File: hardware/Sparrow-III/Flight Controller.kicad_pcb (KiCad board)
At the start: 4 copper layers, 40 x 40 mm, 89 parts

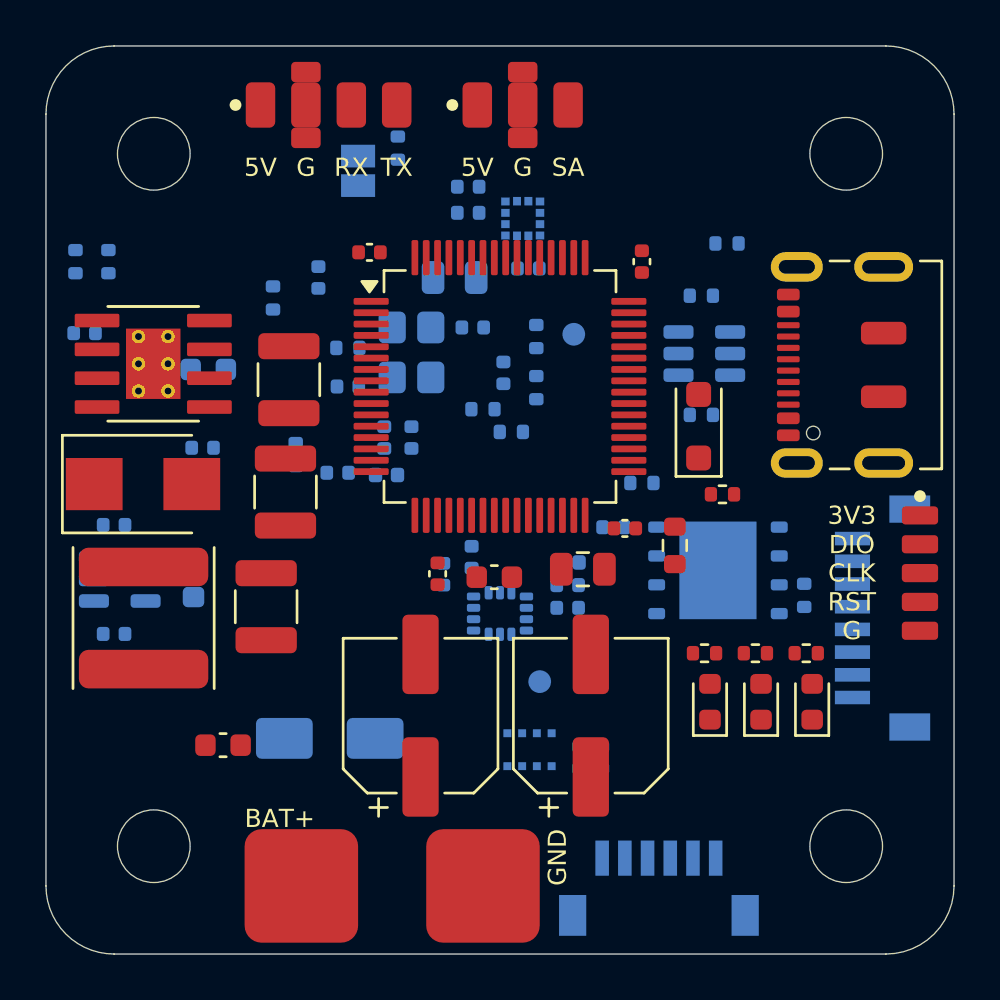
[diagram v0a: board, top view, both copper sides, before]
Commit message: WIP: uncommitted changes, moved to the cloud
Snapshot of the working tree the Claude desktop app took to continue
this session in the cloud. It was never committed on the desktop; fold
it into your next commit (git commit --amend) or unstage it
(git reset --mixed HEAD~1) before committing for real.
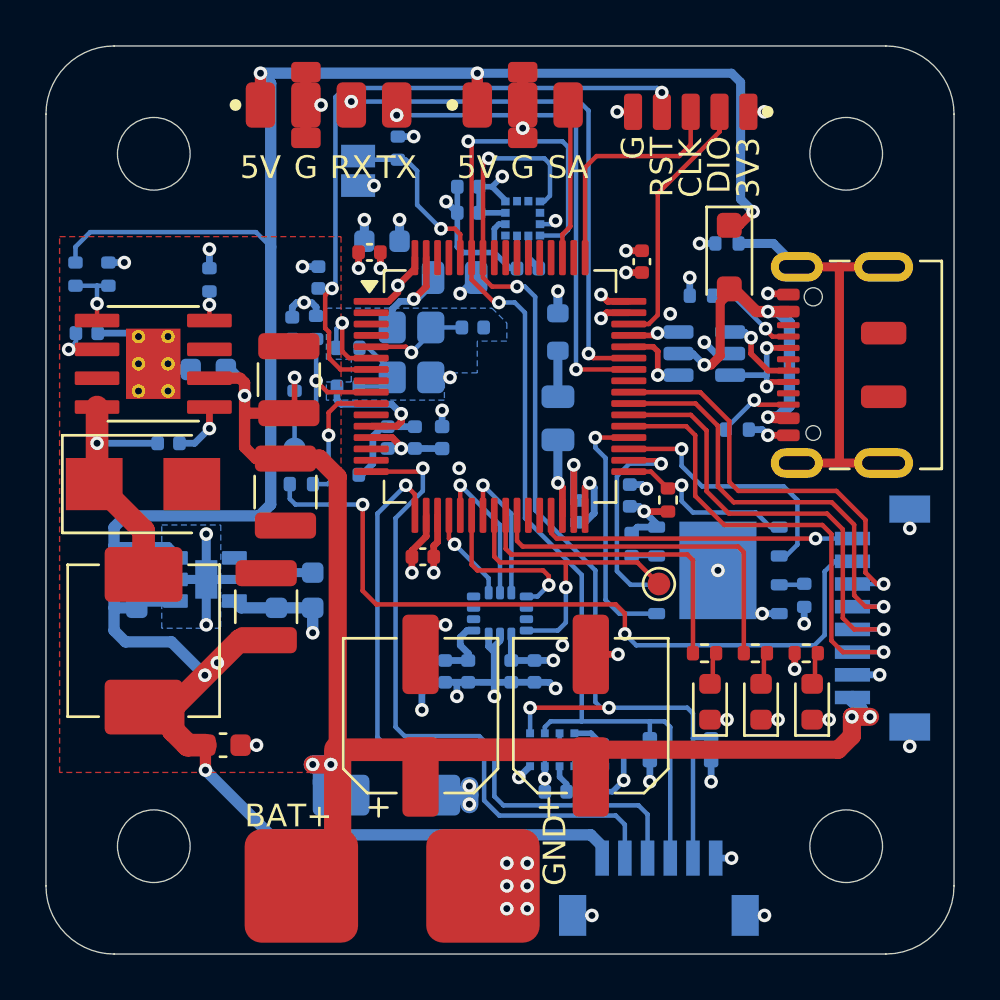
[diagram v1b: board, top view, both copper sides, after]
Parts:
- C_BUCK_OUT1: value 47uF -> 100uF
- C_LDO_IN1, C_LDO_OUT1: value 1uF -> 2.2uF; footprint Capacitor_SMD:C_0402_1005Metric -> Capacitor_SMD:C_0603_1608Metric
- C_MAG_BULK1: value 10uF -> 22uF
- C_VCAP1, C_VDD3, C_VDD_BULK1, R_VCAP_ESR1: moved to B.Cu
- D_TVS1: value SMAJ28A -> SMAJ26A
- L_BUCK1: footprint SparrowHawk:L_Sunlord_SWPA6028S -> SparrowHawk:L_Vishay_IHLP-2525CZ-01
- TP_IMU_INT_0: moved to F.Cu
- U_BARO1: value DPS310 -> DPS368
- U_LDO1: value AP2112K-3.3TRG1 -> TLV75533PDYDR; footprint Package_TO_SOT_SMD:SOT-23-5 -> SparrowHawk:SOT-23-5_ThermalPad_TI_DYD0005A
- Y_HSE1: value 8MHz CL=10pF ESR<150R -> 8MHz
- moved J_SWD1 22.7 mm to (158.4, 82.9), turned to 180 degrees
- moved R_I2C_SDA1 16.7 mm to (156.6, 111.0), turned to -90 degrees
- moved R_I2C_SCL1 16.5 mm to (159.3, 111.0), turned to 90 degrees
- moved C_VDD_BULK1 15.6 mm to (144.8, 88.6), turned to 180 degrees
- moved TP_VBAT_ADC_0 13.3 mm to (140.9, 97.8)
- moved R_VBAT_D1 11.0 mm to (140.9, 95.7)
- moved R_VCAP_ESR1 10.7 mm to (152.6, 92.6)
- moved R_VBAT_D2 10.1 mm to (141.9, 92.4)
- moved C_VBAT_ADC1 9.51 mm to (140.8, 92.4)
- moved FB_IMU1 8.03 mm to (146.6, 107.5), turned to -90 degrees
- moved D_USB_VBUS1 7.57 mm to (160.1, 89.3), turned to -90 degrees
- moved C_LDO_OUT1 7.40 mm to (140.2, 104.0), turned to 90 degrees
- moved TP_IMU_INT_0 6.79 mm to (157.0, 103.7)
- moved C_VCAP1 6.74 mm to (152.6, 96.4), turned to 90 degrees
- moved C_IMU_VDD1 6.08 mm to (147.6, 107.5), turned to -90 degrees
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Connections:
- U_LDO1 pad 4: GND -> unconnected-(U_LDO1-NC-Pad4)
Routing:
- net +5V: track 0.00 -> 113.4 mm, vias 0 -> 6
- net GND: track 0.00 -> 98.5 mm, vias 0 -> 57
- net VBAT: track 0.00 -> 59.5 mm, vias 0 -> 6
- net /MCU Core/I2C1_SDA: track 0.00 -> 50.2 mm, vias 0 -> 2
- net /MCU Core/I2C1_SCL: track 0.00 -> 48.0 mm, vias 0 -> 4
- net +3V3: track 0.00 -> 42.9 mm, vias 0 -> 22
- net /Interfaces&IO/ESC_CURR_IN: track 0.00 -> 34.0 mm, vias 0 -> 2
- net /Interfaces&IO/GPS_TX: track 0.00 -> 30.0 mm, vias 0 -> 1
- net /MCU Core/NRST: track 0.00 -> 29.0 mm, vias 0 -> 2
- net /Interfaces&IO/GPS_RX: track 0.00 -> 28.2 mm, vias 0 -> 1
- net /Interfaces&IO/RC_RX: track 0.00 -> 23.2 mm, vias 0 -> 2
- net /Interfaces&IO/RC_TX: track 0.00 -> 21.2 mm, vias 0 -> 2
- net /Interfaces&IO/M1: track 0.00 -> 21.0 mm, vias 0 -> 1
- net /Interfaces&IO/M2: track 0.00 -> 20.4 mm, vias 0 -> 1
- net /Interfaces&IO/M3: track 0.00 -> 19.7 mm, vias 0 -> 1
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- added copper zone on In2.Cu, net +3V3
- added copper zone on B.Cu, net GND
- added copper zone on F.Cu, net GND
- added copper zone on In1.Cu, net GND
- added copper zone on In2.Cu, net GND
